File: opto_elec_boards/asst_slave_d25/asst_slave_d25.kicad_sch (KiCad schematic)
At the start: 37 parts, among them J1 FromMainBoard, J2 PID_Gain_OK, J3 PID_Int_OK, J4 PID_Der_OK, J5 CLOSE, U1 TL084, U2 TL084

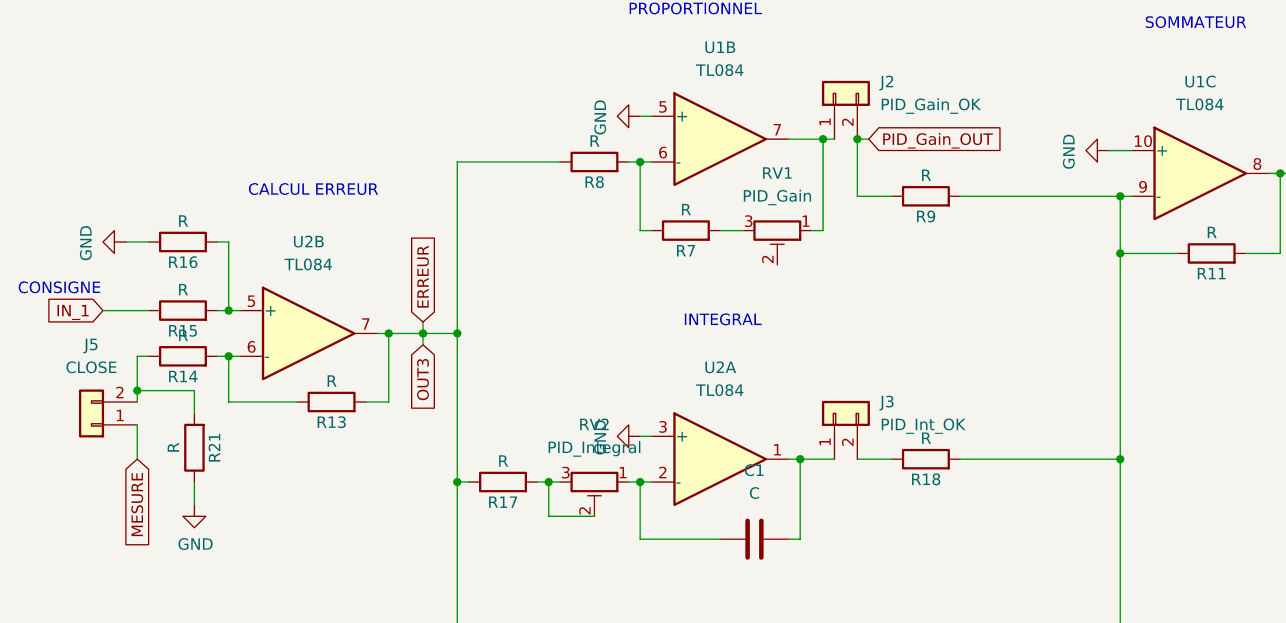
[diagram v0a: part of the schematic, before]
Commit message: Add Opto Board / Illuminance Control loop
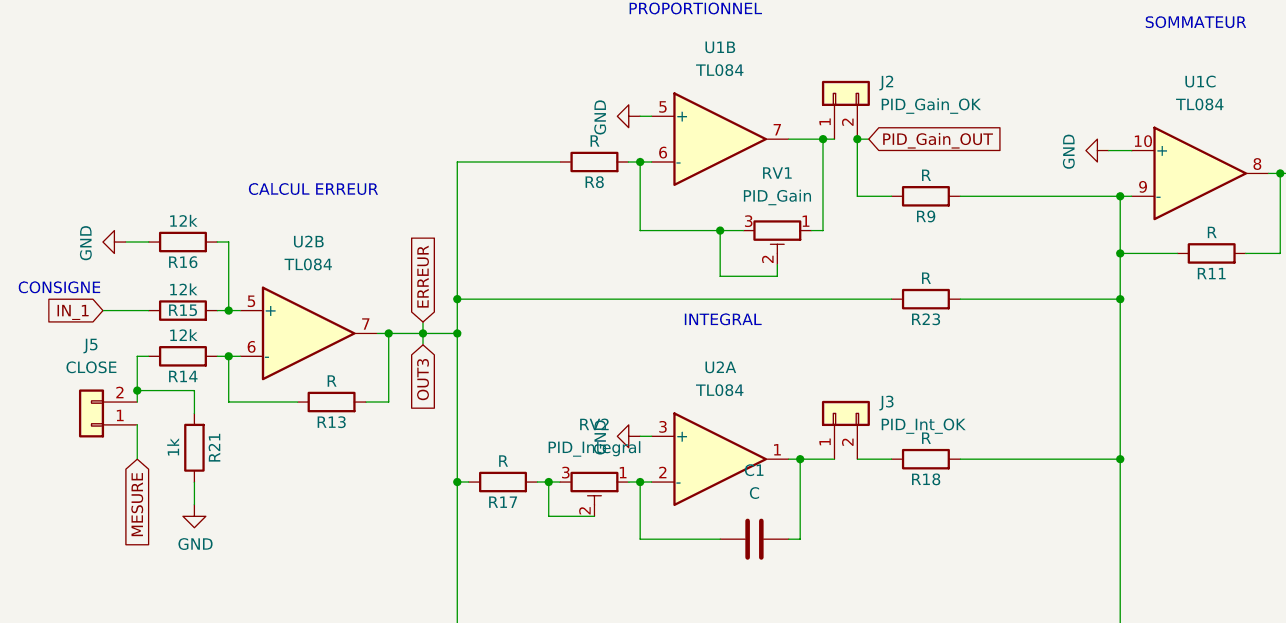
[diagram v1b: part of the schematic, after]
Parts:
- removed R7: R, symbol Device:R
- added R23: R, Resistor_THT:R_Axial_DIN0207_L6.3mm_D2.5mm_P10.16mm_Horizontal, symbol Device:R
- C1, C2: footprint (none) -> LEnsE_devices:C_R_Multi
- J2, J3, J4, J5: footprint (none) -> Connector_PinSocket_2.54mm:PinSocket_1x02_P2.54mm_Vertical
- R10, R11, R12, R13, R17, R18, R19, R20, R8, R9: footprint (none) -> Resistor_THT:R_Axial_DIN0207_L6.3mm_D2.5mm_P10.16mm_Horizontal
- R14, R15, R16: value R -> 12k; footprint (none) -> Resistor_THT:R_Axial_DIN0207_L6.3mm_D2.5mm_P10.16mm_Horizontal
- R21: value R -> 1k; footprint (none) -> Resistor_THT:R_Axial_DIN0207_L6.3mm_D2.5mm_P10.16mm_Horizontal
- R22, R5, R6: footprint Resistor_THT:R_Axial_DIN0309_L9.0mm_D3.2mm_P12.70mm_Horizontal -> Resistor_THT:R_Axial_DIN0207_L6.3mm_D2.5mm_P10.16mm_Horizontal
- RV1, RV2, RV3: footprint (none) -> Potentiometer_THT:Potentiometer_Bourns_3386P_Vertical
- U1, U2: footprint (none) -> Package_DIP:DIP-14_W7.62mm_Socket_LongPads
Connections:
- net ERREUR: now also R23.1
- net at R11.1, R18.2, R20.2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: now also R23.2
- net at R8.2, U1.6 (-): now also RV1.2, RV1.3

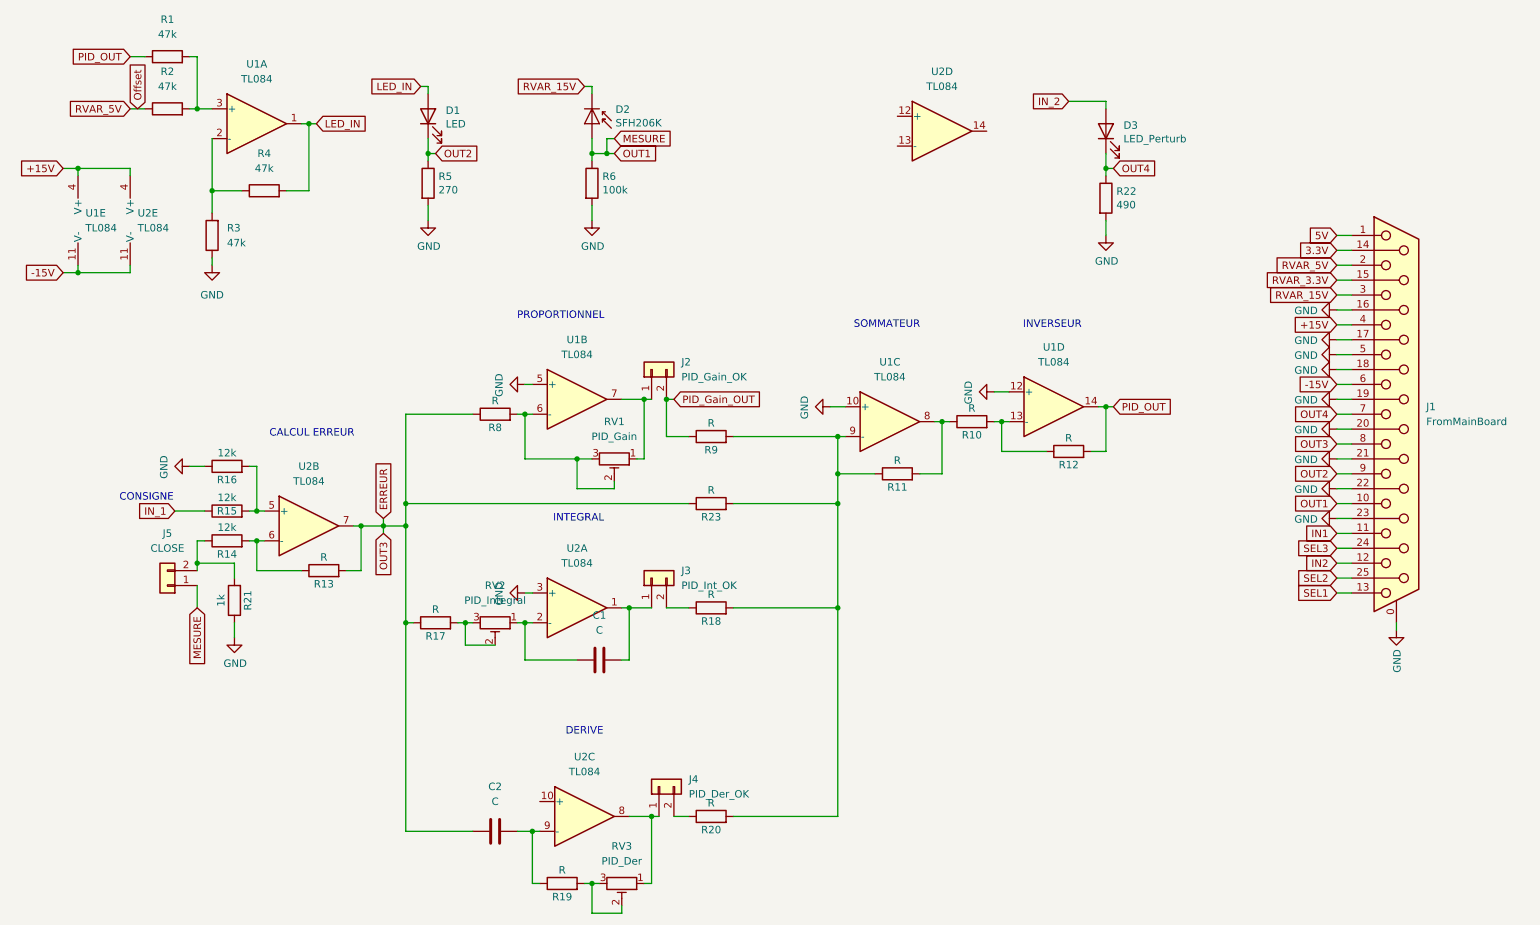
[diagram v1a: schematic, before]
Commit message: Update Opto Board / Illuminance closed loop system
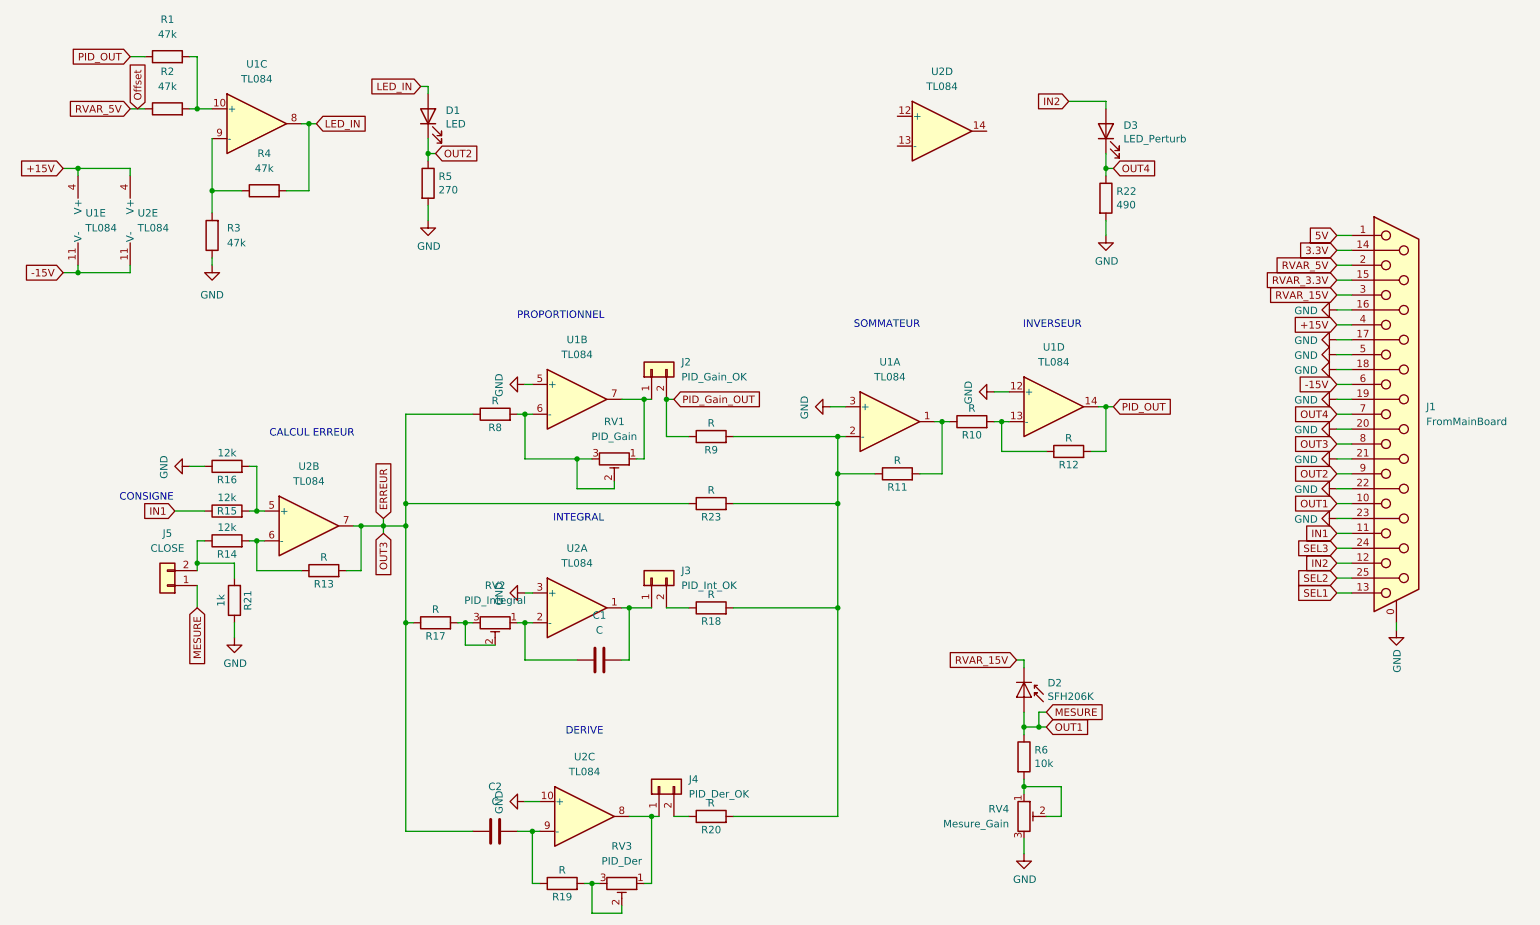
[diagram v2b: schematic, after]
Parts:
- added RV4: Mesure_Gain, Potentiometer_THT:Potentiometer_Bourns_3386P_Vertical, symbol Device:R_Potentiometer_Trim
- D1: footprint LED_THT:LED_D5.0mm_Horizontal_O3.81mm_Z9.0mm -> LED_THT:LED_D10.0mm
- R6: value 100k -> 10k
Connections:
- net IN_1 is gone; now on net IN1: R15.1
- net IN_2 is gone; now on net IN2: D3.2 (A)
- net GND: now also U1.3 (+), U2.10 (+), RV4.3; no longer R6.2, U1.10 (+)
- net LED_IN: now also U1.8; no longer U1.1
- net at R11.1, R18.2, R20.2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: now also U1.2 (-); no longer U1.9 (-)
- net at R10.1, R11.2: now also U1.1; no longer U1.8
- net at R1.2, R2.2: now also U1.10 (+); no longer U1.3 (+)
- net at R3.2, R4.1: now also U1.9 (-); no longer U1.2 (-)
- new net: R6.2, RV4.1, RV4.2
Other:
- moved on the sheet: D2, R6, U1A, U1C

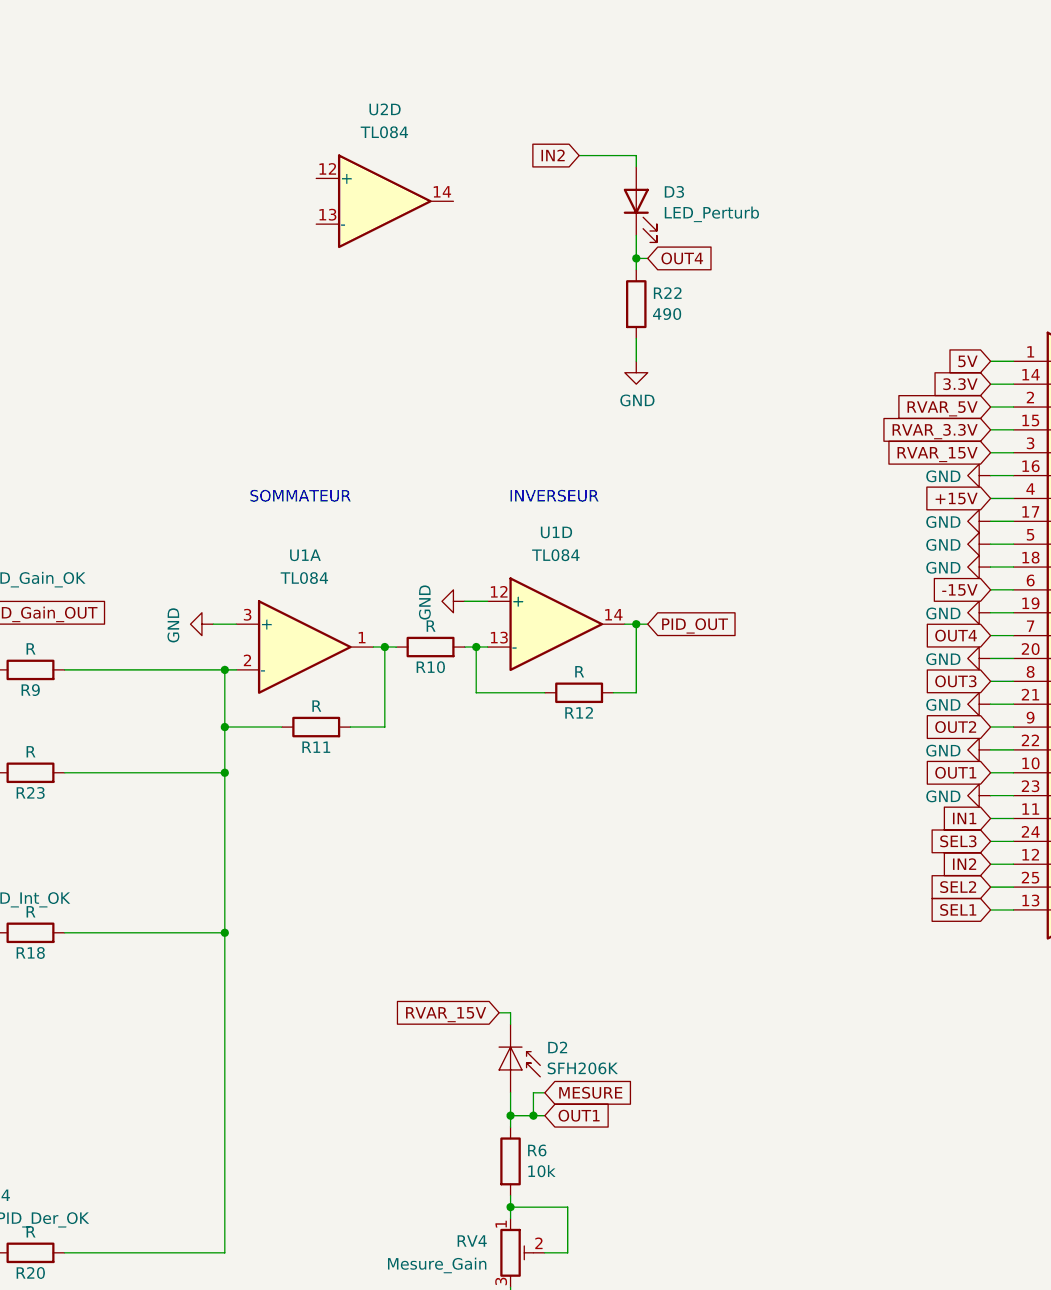
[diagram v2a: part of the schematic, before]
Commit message: Update Opto Board / Update Illuminance Control - analog circuit PID
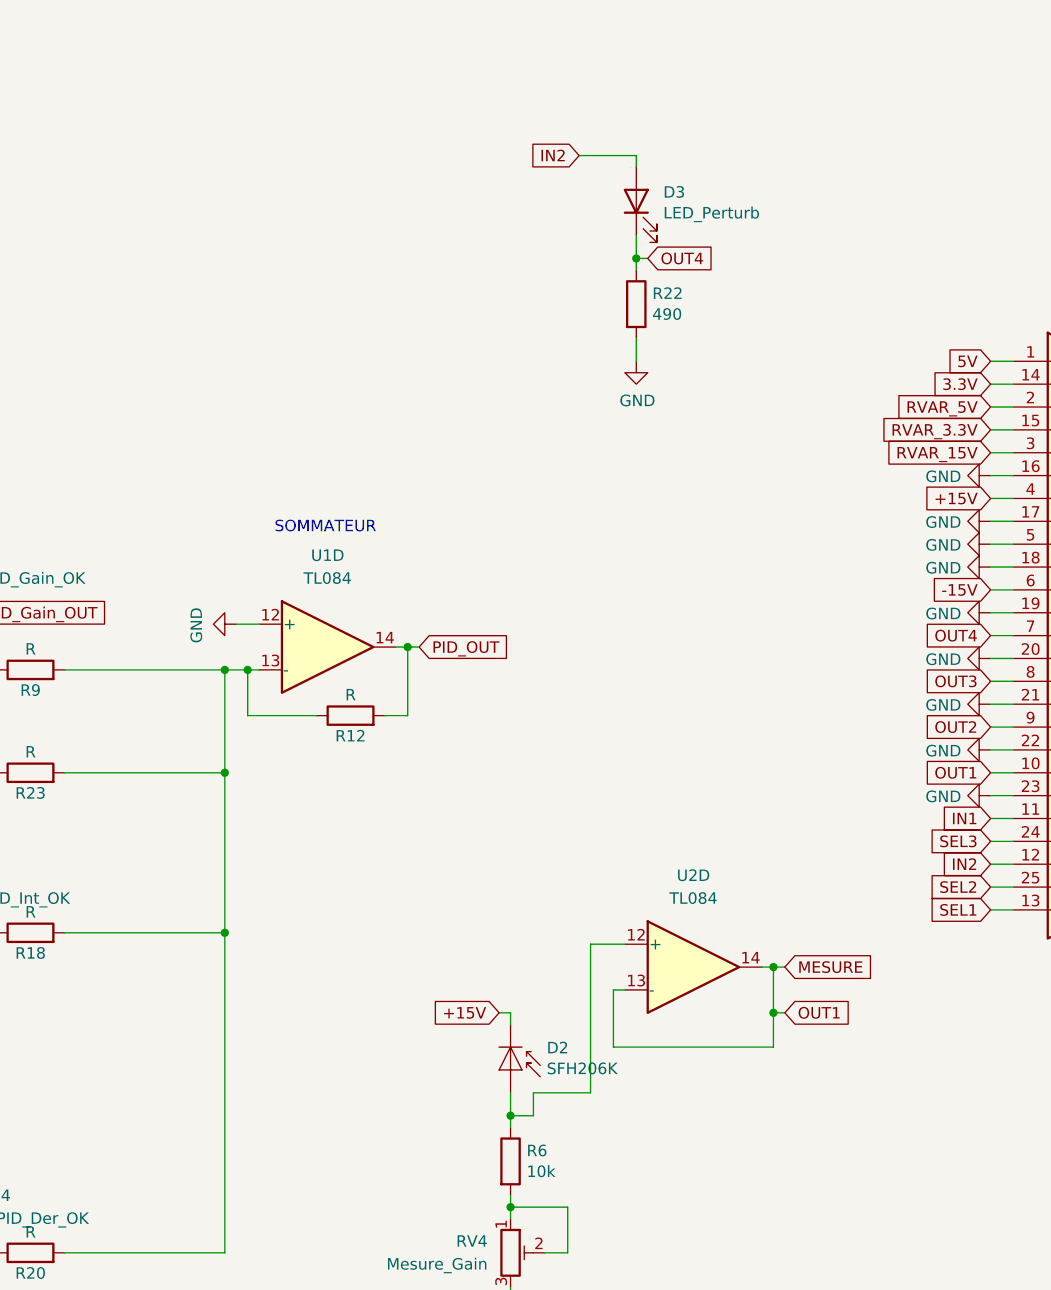
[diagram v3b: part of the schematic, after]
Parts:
- removed R10, R11: R, Resistor_THT:R_Axial_DIN0207_L6.3mm_D2.5mm_P10.16mm_Horizontal, symbol Device:R
- removed unit 1 of U1
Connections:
- net +15V: now also D2.1 (K)
- net MESURE: now also U2.13 (-), U2.14; no longer D2.2 (A), R6.1
- net RVAR_15V: no longer D2.1 (K)
- net at R18.2, R20.2, R23.2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: now also R12.1, U1.13 (-)
- net at U2.12 (+): now also D2.2 (A), R6.1
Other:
- note removed: "INVERSEUR"
- moved on the sheet: R12, U1D, U2D
